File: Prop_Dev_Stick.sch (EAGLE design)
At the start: 52 parts, among them J1 10118193-0001LF, J3 M20-7822046, J4 M20-7822046, U1 P8X32A-Q44, U2 FT230XQ-R, U4 CAT24C512WI-GT3, U5 AD7999YRJZ-1500RL7, U6 TS2937CW33, U8 TPS2115ADRBR, X1 ATS060CSM-1

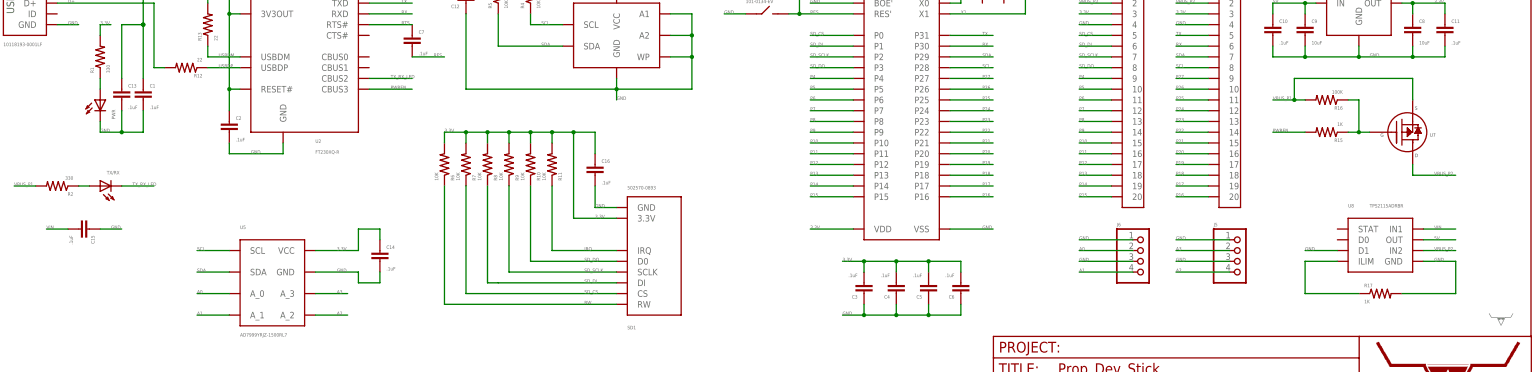
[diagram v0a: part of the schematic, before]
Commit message: Fixed Values on a couple parts. Added BOM.txt
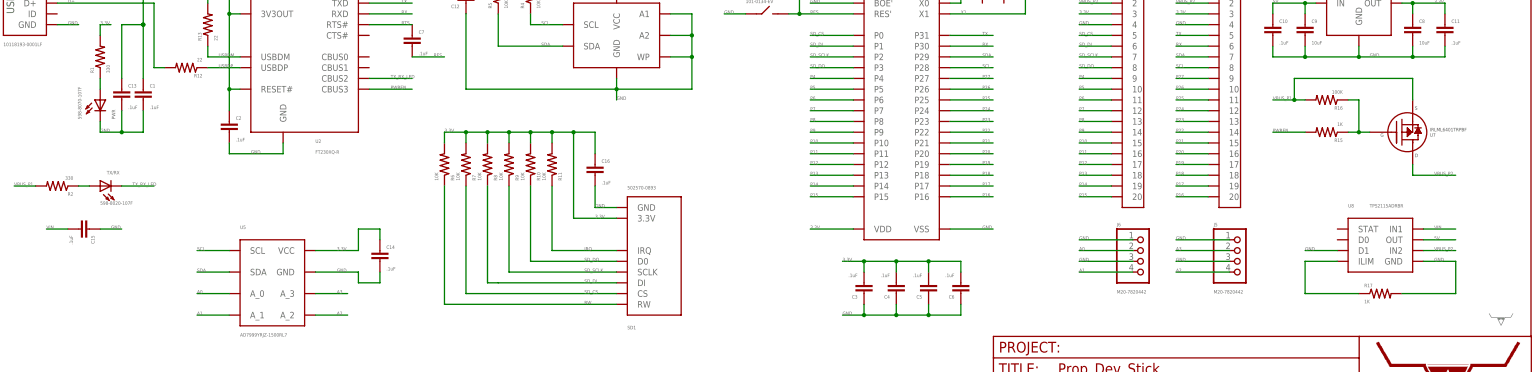
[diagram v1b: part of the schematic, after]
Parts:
- J5, J6: value (none) -> M20-7820442
- L1: value MI0603K300R-10 -> MI0603K300R-10
- PWR: value (none) -> 598-8070-107F
- TX/RX: value (none) -> 598-8020-107F
- U7: value (none) -> IRLML6401TRPBF
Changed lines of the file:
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@@
 </part>
 <part name="X1" library="PP_FreqCtrl" deviceset="CRYSTAL" device="HC-49" value="ATS060CSM-1"/>
-<part name="PWR" library="led" deviceset="LED" device="SML0603"/>
+<part name="PWR" library="led" deviceset="LED" device="SML0603" value="598-8070-107F"/>
 <part name="U2" library="PP_DigitalIC" deviceset="FT230X" device="QFN-16" value="FT230XQ-R"/>
 <part name="C1" library="PP_Passives" deviceset="CAPACITOR_NON_POLAR" device="0402" value=".1uF"/>
 <part name="C2" library="PP_Passives" deviceset="CAPACITOR_NON_POLAR" device="0402" value=".1uF"/>
 <part name="R1" library="PP_Passives" deviceset="RESISTOR" device="0402" value="330"/>
-<part name="TX/RX" library="led" deviceset="LED" device="SML0603"/>
+<part name="TX/RX" library="led" deviceset="LED" device="SML0603" value="598-8020-107F "/>
 <part name="R2" library="PP_Passives" deviceset="RESISTOR" device="0402" value="330"/>
 <part name="C3" library="PP_Passives" deviceset="CAPACITOR_NON_POLAR" device="0402" value=".1uF"/>
@@
 <part name="C11" library="PP_Passives" deviceset="CAPACITOR_NON_POLAR" device="0402" value=".1uF"/>
 <part name="U6" library="PP_PowerIC" deviceset="FIXED_VOLTAGE_REG" device="SOT-223" value="TS2937CW33"/>
-<part name="U7" library="PP_DiscreteSemi" deviceset="MOSFET_P-CHANNEL_SINGLE" device="SOT-23"/>
+<part name="U7" library="PP_DiscreteSemi" deviceset="MOSFET_P-CHANNEL_SINGLE" device="SOT-23" value="IRLML6401TRPBF"/>
 <part name="R15" library="PP_Passives" deviceset="RESISTOR" device="0402" value="1K"/>
 <part name="R16" library="PP_Passives" deviceset="RESISTOR" device="0402" value="100K"/>
-<part name="L1" library="PP_Passives" deviceset="RESISTOR" device="0603" value="  MI0603K300R-10"/>
+<part name="L1" library="PP_Passives" deviceset="RESISTOR" device="0603" value="MI0603K300R-10"/>
 <part name="C13" library="PP_Passives" deviceset="CAPACITOR_NON_POLAR" device="0402" value=".1uF"/>
 <part name="U$2" library="PP_Aesthetics" deviceset="LHE_LOGO" device="LHE_LOGO"/>
-<part name="J5" library="PP_Connectors" deviceset="PH_1X04" device="HEADER_PTH_ROUND"/>
-<part name="J6" library="PP_Connectors" deviceset="PH_1X04" device="HEADER_PTH_ROUND"/>
+<part name="J5" library="PP_Connectors" deviceset="PH_1X04" device="HEADER_PTH_ROUND" value="M20-7820442"/>
+<part name="J6" library="PP_Connectors" deviceset="PH_1X04" device="HEADER_PTH_ROUND" value="M20-7820442"/>
 <part name="U5" library="PP_DigitalIC" deviceset="AD799X" device="SOT-23-8" value="AD7999YRJZ-1500RL7"/>
 <part name="C14" library="PP_Passives" deviceset="CAPACITOR_NON_POLAR" device="0402" value=".1uF"/>
@@
 <instance part="PWR" gate="G$1" x="-355.6" y="228.6" smashed="yes">
 <attribute name="NAME" x="-352.044" y="224.028" size="0.8128" layer="95" font="vector" rot="R90"/>
-<attribute name="VALUE" x="-349.885" y="224.028" size="1.778" layer="96" rot="R90"/>
+<attribute name="VALUE" x="-360.045" y="224.028" size="0.8128" layer="96" font="vector" rot="R90"/>
 </instance>
 <instance part="U2" gate="G$1" x="-307.34" y="241.3"/>
@@
 <instance part="TX/RX" gate="G$1" x="-355.6" y="208.28" smashed="yes" rot="R90">
 <attribute name="NAME" x="-351.028" y="211.836" size="0.8128" layer="95" font="vector" rot="R180"/>
-<attribute name="VALUE" x="-351.028" y="213.995" size="1.778" layer="96" rot="R180"/>
+<attribute name="VALUE" x="-355.6" y="203.835" size="0.8128" layer="96" font="vector"/>
 </instance>
 <instance part="R2" gate="G$1" x="-365.76" y="208.28" rot="R180"/>

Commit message: Finished REV3!!!
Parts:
- removed U8: TPS2115ADRBR, PP_PowerIC:TPS2115SON-8
- added U3: TPS2111APWR, PP_PowerIC:TPS2111SON-8
- C1, C10, C11, C12, C13, C14, C15, C16, C2, C3, C4, C5, C6, C7: device PP_Passives:CAPACITOR_NON_POLAR0402 -> PP_Passives:CAPACITOR_NON_POLAR0603
- L1: device PP_Passives:RESISTOR0603 -> PP_Passives:INDUCTOR0603
- PWR: value 598-8070-107F -> 598-8020-107F; device led:LEDSML0603 -> PP_LED:LED_SINGLE0805
- R1, R10, R11, R12, R13, R14, R15, R16, R17, R2, R4, R5, R6, R7, R8, R9: device PP_Passives:RESISTOR0402 -> PP_Passives:RESISTOR0603
- TX/RX: device led:LEDSML0603 -> PP_LED:LED_SINGLE0805
- U$1: REVNUM REV 2 -> REV 3
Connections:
- net 3.3V: now also J5.2, J6.2
- net 3V3OUT: now also R2.2
- net 5V: now also U3.OUT; no longer U8.OUT
- net A0: now also J6.4; no longer J6.2
- net A1: now also J6.3; no longer J6.4
- net A2: now also J5.3; no longer J5.4
- net A3: now also J5.4; no longer J5.2
- net GND: now also PWR.CATHODE, U3.D1, U3.GND; no longer J5.3, J6.3, PWR.C, U8.D1, U8.GND
- net N$1: now also PWR.ANODE; no longer PWR.A
- net N$2: now also TX/RX.ANODE; no longer TX/RX.A
- net N$7: now also U3.ILIM; no longer U8.ILIM
- net TX_RX_LED: now also TX/RX.CATHODE; no longer TX/RX.C
- net VBUS: now also L1.P$1; no longer L1.2
- net VBUS_P1: now also L1.P$2; no longer L1.1, R2.2
- net VBUS_P2: now also U3.IN2; no longer U8.IN2
- net VIN: now also U3.IN1, U3.VSNS; no longer U8.IN1
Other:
- moved on the sheet: J1, R1

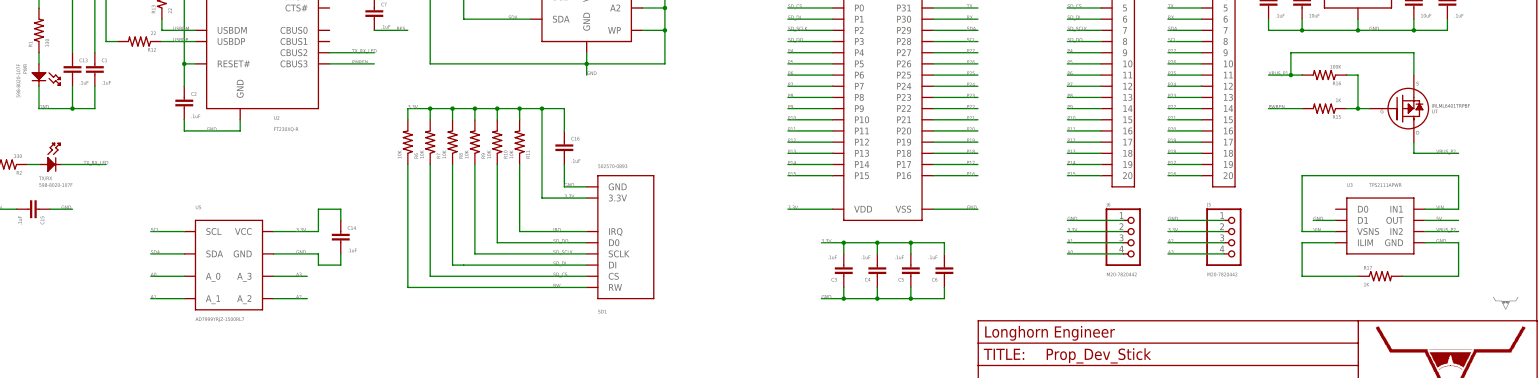
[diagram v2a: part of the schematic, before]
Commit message: Added power switching for LDO Voltage Dropout.
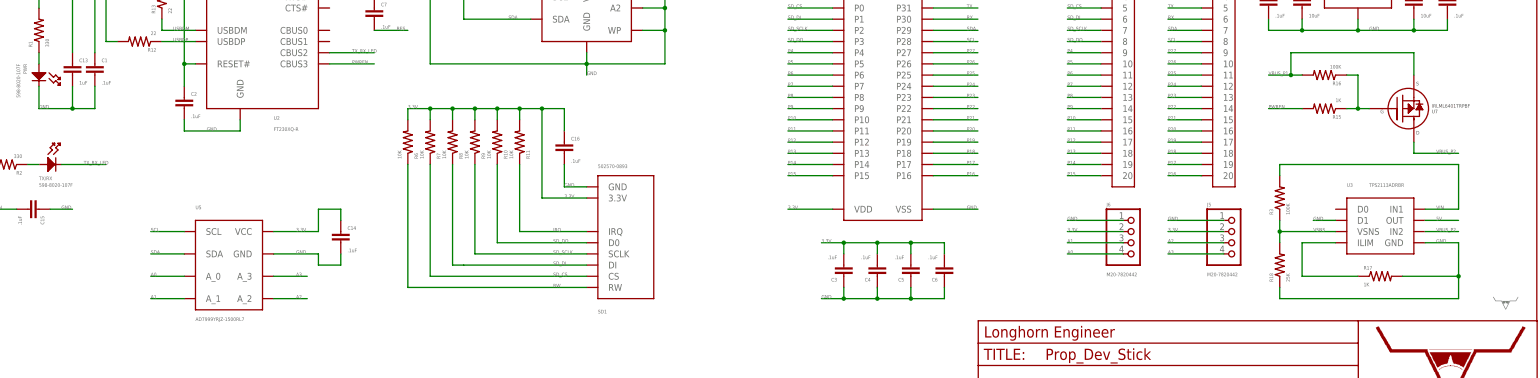
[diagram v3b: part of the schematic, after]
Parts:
- added R18: 25K, PP_Passives:RESISTOR0603
- added R3: 100K, PP_Passives:RESISTOR0603
- C13: value .1uF -> 1uF
- U$1: REVNUM REV 3 -> REV 4
- U3: value TPS2111APWR -> TPS2113ADRBR
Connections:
- new net VSNS: R18.2, R3.1, U3.VSNS
- net GND: now also R18.1
- net VIN: now also R3.2; no longer U3.VSNS

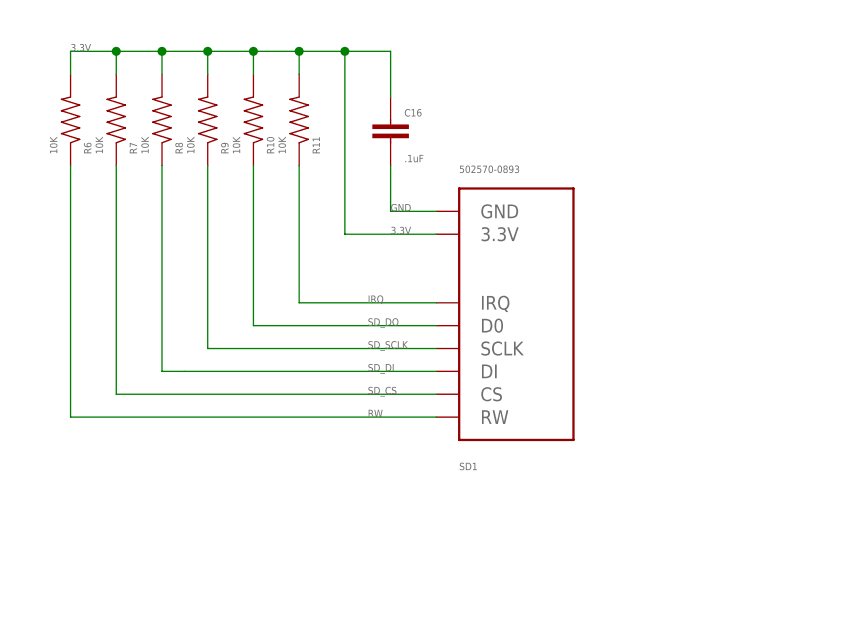
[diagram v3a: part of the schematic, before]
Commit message: Changed SD Card Slot.
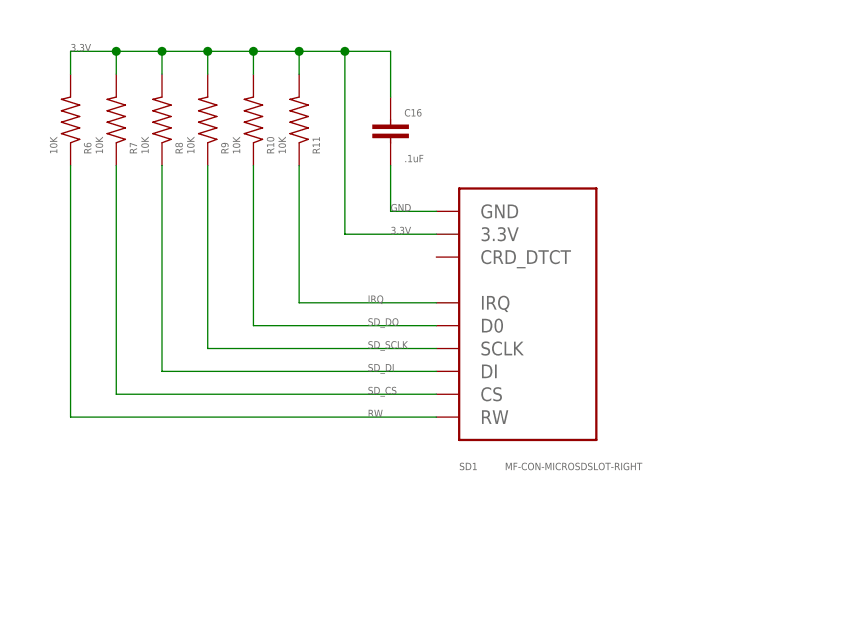
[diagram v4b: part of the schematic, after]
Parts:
- SD1: value 502570-0893 -> MF-CON-MICROSDSLOT-RIGHT; device PP_Connectors:SD_CARD502570-0893 -> MF_Connectors:SD_CARD_SLOTRIGHT
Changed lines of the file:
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@@
 <part name="C12" library="PP_Passives" deviceset="CAPACITOR_NON_POLAR" device="0603" value=".1uF"/>
 <part name="J1" library="PP_Connectors" deviceset="USB" device="10118193-0001LF" value="10118193-0001LF"/>
-<part name="SD1" library="PP_Connectors" deviceset="SD_CARD" device="502570-0893" value="502570-0893"/>
 <part name="R6" library="PP_Passives" deviceset="RESISTOR" device="0603" value="10K"/>
 <part name="R7" library="PP_Passives" deviceset="RESISTOR" device="0603" value="10K"/>
@@
 <part name="R3" library="PP_Passives" deviceset="RESISTOR" device="0603" value="100K"/>
 <part name="R18" library="PP_Passives" deviceset="RESISTOR" device="0603" value="25K"/>
+<part name="SD1" library="MF_Connectors" deviceset="SD_CARD_SLOT" device="RIGHT" value="MF-CON-MICROSDSLOT-RIGHT"/>
 </parts>
 <sheets>
@@
 <instance part="C12" gate="G$1" x="-269.24" y="251.46" rot="R180"/>
 <instance part="J1" gate="G$1" x="-378.46" y="251.46"/>
-<instance part="SD1" gate="G$1" x="-228.6" y="195.58" rot="MR180"/>
 <instance part="R6" gate="G$1" x="-274.32" y="213.36" rot="MR90"/>
 <instance part="R7" gate="G$1" x="-269.24" y="213.36" rot="MR90"/>
@@
 <instance part="R3" gate="G$1" x="-76.2" y="200.66" rot="R90"/>
 <instance part="R18" gate="G$1" x="-76.2" y="185.42" rot="R90"/>
+<instance part="SD1" gate="G$1" x="-223.52" y="190.5" rot="MR180"/>
 </instances>
 <busses>
@@
 </segment>
 <segment>
-<pinref part="SD1" gate="G$1" pin="GND"/>
 <wire x1="-233.68" y1="203.2" x2="-238.76" y2="203.2" width="0.1524" layer="91"/>
 <label x="-238.76" y="203.2" size="0.8128" layer="95" font="vector"/>
 <pinref part="C16" gate="G$1" pin="2"/>
 <wire x1="-238.76" y1="208.28" x2="-238.76" y2="203.2" width="0.1524" layer="91"/>
+<pinref part="SD1" gate="G$1" pin="GND"/>
 </segment>
 <segment>
@@
 <wire x1="-248.92" y1="220.98" x2="-243.84" y2="220.98" width="0.1524" layer="91"/>
 <wire x1="-243.84" y1="220.98" x2="-243.84" y2="200.66" width="0.1524" layer="91"/>
-<pinref part="SD1" gate="G$1" pin="3.3V"/>
 <wire x1="-243.84" y1="200.66" x2="-233.68" y2="200.66" width="0.1524" layer="91"/>
 <label x="-238.76" y="200.66" size="0.8128" layer="95" font="vector"/>
@@
 <junction x="-254" y="220.98"/>
 <junction x="-248.92" y="220.98"/>
+<pinref part="SD1" gate="G$1" pin="3.3V"/>
 </segment>
 <segment>
@@
 <net name="SD_SCLK" class="0">
 <segment>
-<pinref part="SD1" gate="G$1" pin="SCLK"/>
 <wire x1="-233.68" y1="187.96" x2="-259.08" y2="187.96" width="0.1524" layer="91"/>
 <label x="-241.3" y="187.96" size="0.8128" layer="95" font="vector"/>
 <pinref part="R9" gate="G$1" pin="1"/>
 <wire x1="-259.08" y1="187.96" x2="-259.08" y2="208.28" width="0.1524" layer="91"/>
+<pinref part="SD1" gate="G$1" pin="SCLK"/>
 </segment>
 <segment>
@@
 <net name="SD_DI" class="0">
 <segment>
-<pinref part="SD1" gate="G$1" pin="DI"/>
-<wire x1="-233.68" y1="185.42" x2="-261.62" y2="185.42" width="0.1524" layer="91"/>
+<wire x1="-233.68" y1="185.42" x2="-264.16" y2="185.42" width="0.1524" layer="91"/>
 <label x="-241.3" y="185.42" size="0.8128" layer="95" font="vector"/>
 <pinref part="R8" gate="G$1" pin="1"/>
-<wire x1="-261.62" y1="185.42" x2="-264.16" y2="185.42" width="0.1524" layer="91"/>
 <wire x1="-264.16" y1="185.42" x2="-264.16" y2="208.28" width="0.1524" layer="91"/>
+<pinref part="SD1" gate="G$1" pin="DI"/>
 </segment>
 <segment>
@@
 <net name="SD_CS" class="0">
 <segment>
-<pinref part="SD1" gate="G$1" pin="CS"/>
 <wire x1="-233.68" y1="182.88" x2="-269.24" y2="182.88" width="0.1524" layer="91"/>
 <label x="-241.3" y="182.88" size="0.8128" layer="95" font="vector"/>
 <pinref part="R7" gate="G$1" pin="1"/>
 <wire x1="-269.24" y1="208.28" x2="-269.24" y2="182.88" width="0.1524" layer="91"/>
+<pinref part="SD1" gate="G$1" pin="CS"/>
 </segment>
 <segment>
@@
 <net name="IRQ" class="0">
 <segment>
-<pinref part="SD1" gate="G$1" pin="IRQ"/>
 <wire x1="-233.68" y1="193.04" x2="-248.92" y2="193.04" width="0.1524" layer="91"/>
 <label x="-241.3" y="193.04" size="0.8128" layer="95" font="vector"/>
 <pinref part="R11" gate="G$1" pin="1"/>
 <wire x1="-248.92" y1="193.04" x2="-248.92" y2="208.28" width="0.1524" layer="91"/>
+<pinref part="SD1" gate="G$1" pin="IRQ"/>
 </segment>
 </net>
 <net name="RW" class="0">
 <segment>
-<pinref part="SD1" gate="G$1" pin="RW"/>
 <wire x1="-233.68" y1="180.34" x2="-274.32" y2="180.34" width="0.1524" layer="91"/>
 <label x="-241.3" y="180.34" size="0.8128" layer="95" font="vector"/>
 <pinref part="R6" gate="G$1" pin="1"/>
 <wire x1="-274.32" y1="180.34" x2="-274.32" y2="208.28" width="0.1524" layer="91"/>
+<pinref part="SD1" gate="G$1" pin="RW"/>
 </segment>
 </net>
 <net name="SD_DO" class="0">
 <segment>
-<pinref part="SD1" gate="G$1" pin="D0"/>
 <wire x1="-233.68" y1="190.5" x2="-254" y2="190.5" width="0.1524" layer="91"/>
 <label x="-241.3" y="190.5" size="0.8128" layer="95" font="vector"/>
 <pinref part="R10" gate="G$1" pin="1"/>
 <wire x1="-254" y1="208.28" x2="-254" y2="190.5" width="0.1524" layer="91"/>
-</segment>
-<segment>
+<pinref part="SD1" gate="G$1" pin="D0"/>
+</segment>
+<segment>
